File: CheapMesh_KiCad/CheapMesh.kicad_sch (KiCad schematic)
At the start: 24 parts, among them J1 Conn_01x02_Pin, J2 Conn_01x09_Pin, J3 USB_A, J4 USB_C, J5 Conn_Coaxial, Q1 UMH3N, U1 L78L33, U2 HT-CT62, U3 AP2112K-3.3

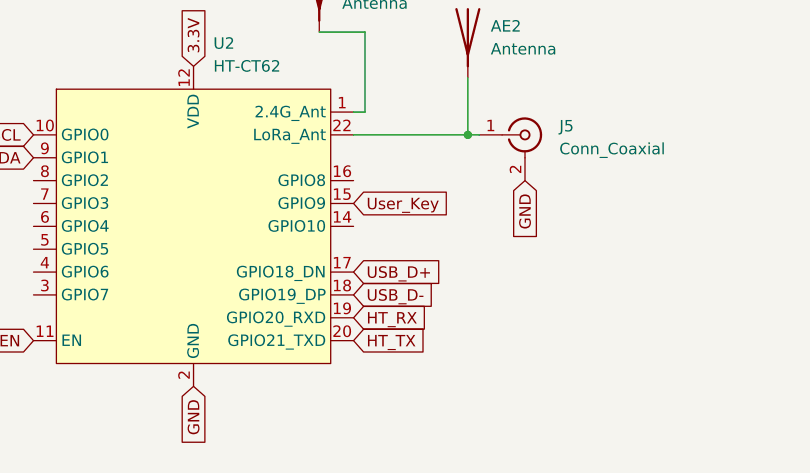
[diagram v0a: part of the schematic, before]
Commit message: update
swapp d+ d-, add gpio 2, PCB v 1.4.4
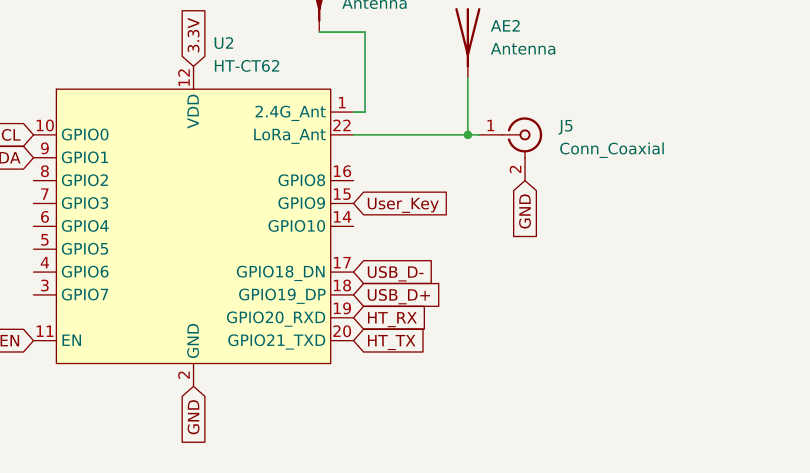
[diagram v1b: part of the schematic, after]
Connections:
- net USB_D+: now also U2.18 (GPIO19_DP); no longer U2.17 (GPIO18_DN)
- net USB_D-: now also U2.17 (GPIO18_DN); no longer U2.18 (GPIO19_DP)
